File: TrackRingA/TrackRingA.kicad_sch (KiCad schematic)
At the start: 14 parts, among them J1 Conn_01x04, U1 TLV493D-A1B6, U2 LIS2DTW12

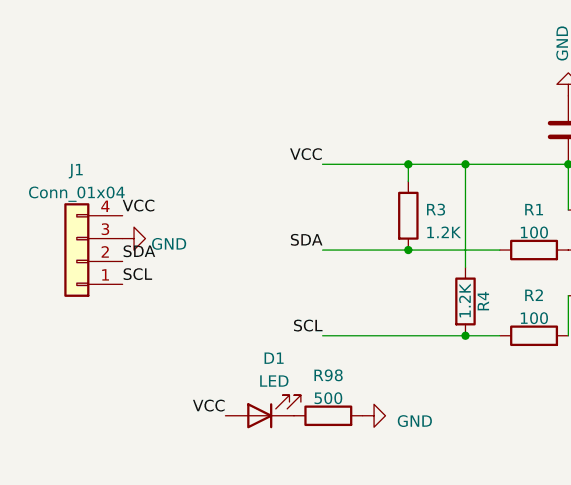
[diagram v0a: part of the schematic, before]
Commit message: Finished BusChain1.1 and added power daisy-chaining option
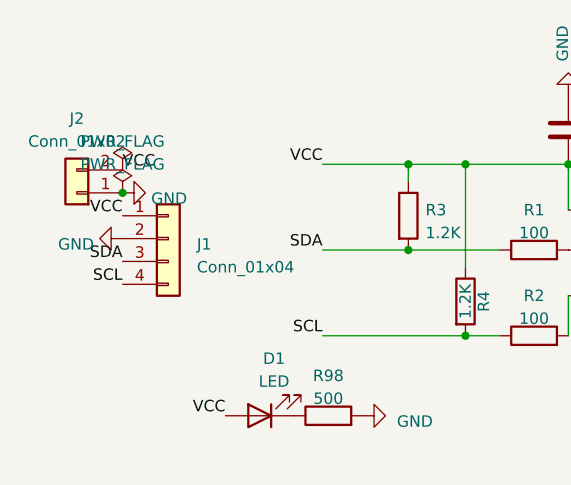
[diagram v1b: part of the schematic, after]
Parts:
- added J2: Conn_01x02, Connector_PinHeader_2.54mm:PinHeader_1x02_P2.54mm_Vertical, symbol Connector_Generic:Conn_01x02
- J1: footprint Connector_PinSocket_2.54mm:PinSocket_1x04_P2.54mm_Horizontal -> Connector_PinHeader_2.54mm:PinHeader_1x04_P2.54mm_Vertical
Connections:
- net GND: now also J1.2 (Pin_2), J2.1 (Pin_1); no longer J1.3 (Pin_3)
- net SCL: now also J1.4 (Pin_4); no longer J1.1 (Pin_1)
- net SDA: now also J1.3 (Pin_3); no longer J1.2 (Pin_2)
- net VCC: now also J1.1 (Pin_1), J2.2 (Pin_2); no longer J1.4 (Pin_4)
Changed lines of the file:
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@@
   (junction (at 92.075 91.44) (diameter 0) (color 0 0 0 0)
   )
+  (junction (at 27.305 31.115) (diameter 0) (color 0 0 0 0)
+  )
   (junction (at 76.2 66.04) (diameter 0) (color 0 0 0 0)
   )
@@
     (effects (font (size 1.27 1.27)) (justify right bottom))
   )
-  (label "SCL" (at 27.305 41.275 0) (fields_autoplaced)
+  (label "SCL" (at 27.305 41.275 180) (fields_autoplaced)
+    (effects (font (size 1.27 1.27)) (justify right bottom))
+  )
+  (label "VCC" (at 38.735 55.88 180) (fields_autoplaced)
+    (effects (font (size 1.27 1.27)) (justify right bottom))
+  )
+  (label "SCL" (at 49.53 46.99 180) (fields_autoplaced)
+    (effects (font (size 1.27 1.27)) (justify right bottom))
+  )
+  (label "SDA" (at 27.305 38.735 180) (fields_autoplaced)
+    (effects (font (size 1.27 1.27)) (justify right bottom))
+  )
+  (label "VCC" (at 88.9 66.04 180) (fields_autoplaced)
+    (effects (font (size 1.27 1.27)) (justify right bottom))
+  )
+  (label "VCC" (at 27.305 28.575 0) (fields_autoplaced)
     (effects (font (size 1.27 1.27)) (justify left bottom))
   )
-  (label "VCC" (at 38.735 55.88 180) (fields_autoplaced)
-    (effects (font (size 1.27 1.27)) (justify right bottom))
-  )
-  (label "SCL" (at 49.53 46.99 180) (fields_autoplaced)
-    (effects (font (size 1.27 1.27)) (justify right bottom))
-  )
-  (label "SDA" (at 27.305 38.735 0) (fields_autoplaced)
-    (effects (font (size 1.27 1.27)) (justify left bottom))
-  )
-  (label "VCC" (at 88.9 66.04 180) (fields_autoplaced)
-    (effects (font (size 1.27 1.27)) (justify right bottom))
-  )
-  (label "VCC" (at 27.305 33.655 0) (fields_autoplaced)
-    (effects (font (size 1.27 1.27)) (justify left bottom))
+  (label "VCC" (at 27.305 33.655 180) (fields_autoplaced)
+    (effects (font (size 1.27 1.27)) (justify right bottom))
+  )
+  (symbol (lib_id "Connector_Generic:Conn_01x04") (at 32.385 36.195 0) (unit 1)
+    (in_bom yes) (on_board yes) (dnp no) (fields_autoplaced)
+    (property "Reference" "J1" (at 35.56 36.83 0)
+      (effects (font (size 1.27 1.27)) (justify left))
+    )
+    (property "Value" "Conn_01x04" (at 35.56 39.37 0)
+      (effects (font (size 1.27 1.27)) (justify left))
+    )
+    (property "Footprint" "Connector_PinHeader_2.54mm:PinHeader_1x04_P2.54mm_Vertical" (at 32.385 36.195 0)
+      (effects (font (size 1.27 1.27)) hide)
+    )
+    (property "Datasheet" "~" (at 32.385 36.195 0)
+      (effects (font (size 1.27 1.27)) hide)
+    )
+    (pin "1")
+    (pin "2")
+    (pin "3")
+    (pin "4")
+    (instances
+      (project "TrackRingA"
+        (path "/1a22a45d-0453-4b94-9e49-dc92af99da64"
+          (reference "J1") (unit 1)
+        )
+      )
+    )
   )
   (symbol (lib_id "Device:R") (at 72.39 76.2 90) (unit 1)
@@
         (path "/1a22a45d-0453-4b94-9e49-dc92af99da64"
           (reference "R7") (unit 1)
+        )
+      )
+    )
+  )
+  (symbol (lib_id "power:GND") (at 27.305 31.115 90) (unit 1)
+    (in_bom yes) (on_board yes) (dnp no) (fields_autoplaced)
+    (property "Reference" "#PWR07" (at 33.655 31.115 0)
+      (effects (font (size 1.27 1.27)) hide)
+    )
+    (property "Value" "GND" (at 30.48 31.75 90)
+      (effects (font (size 1.27 1.27)) (justify right))
+    )
+    (property "Footprint" "" (at 27.305 31.115 0)
+      (effects (font (size 1.27 1.27)) hide)
+    )
+    (property "Datasheet" "" (at 27.305 31.115 0)
+      (effects (font (size 1.27 1.27)) hide)
+    )
+    (pin "1")
+    (instances
+      (project "TrackRingA"
+        (path "/1a22a45d-0453-4b94-9e49-dc92af99da64"
+          (reference "#PWR07") (unit 1)
         )
       )
@@
     )
   )
+  (symbol (lib_id "power:PWR_FLAG") (at 27.305 28.575 0) (unit 1)
+    (in_bom yes) (on_board yes) (dnp no) (fields_autoplaced)
+    (property "Reference" "#FLG01" (at 27.305 26.67 0)
+      (effects (font (size 1.27 1.27)) hide)
+    )
+    (property "Value" "PWR_FLAG" (at 27.305 25.4 0)
+      (effects (font (size 1.27 1.27)))
+    )
+    (property "Footprint" "" (at 27.305 28.575 0)
+      (effects (font (size 1.27 1.27)) hide)
+    )
+    (property "Datasheet" "~" (at 27.305 28.575 0)
+      (effects (font (size 1.27 1.27)) hide)
+    )
+    (pin "1")
+    (instances
+      (project "TrackRingA"
+        (path "/1a22a45d-0453-4b94-9e49-dc92af99da64"
+          (reference "#FLG01") (unit 1)
+        )
+      )
+    )
+  )
   (symbol (lib_id "Device:R") (at 50.165 55.88 90) (unit 1)
     (in_bom yes) (on_board yes) (dnp no) (fields_autoplaced)
@@
         (path "/1a22a45d-0453-4b94-9e49-dc92af99da64"
           (reference "#PWR01") (unit 1)
+        )
+      )
+    )
+  )
+  (symbol (lib_id "power:PWR_FLAG") (at 27.305 31.115 0) (unit 1)
+    (in_bom yes) (on_board yes) (dnp no) (fields_autoplaced)
+    (property "Reference" "#FLG02" (at 27.305 29.21 0)
+      (effects (font (size 1.27 1.27)) hide)
+    )
+    (property "Value" "PWR_FLAG" (at 27.305 27.94 0)
+      (effects (font (size 1.27 1.27)))
+    )
+    (property "Footprint" "" (at 27.305 31.115 0)
+      (effects (font (size 1.27 1.27)) hide)
+    )
+    (property "Datasheet" "~" (at 27.305 31.115 0)
+      (effects (font (size 1.27 1.27)) hide)
+    )
+    (pin "1")
+    (instances
+      (project "TrackRingA"
+        (path "/1a22a45d-0453-4b94-9e49-dc92af99da64"
+          (reference "#FLG02") (unit 1)
+        )
+      )
+    )
+  )
+  (symbol (lib_id "Connector_Generic:Conn_01x02") (at 22.225 31.115 180) (unit 1)
+    (in_bom yes) (on_board yes) (dnp no) (fields_autoplaced)
+    (property "Reference" "J2" (at 22.225 22.86 0)
+      (effects (font (size 1.27 1.27)))
+    )
+    (property "Value" "Conn_01x02" (at 22.225 25.4 0)
+      (effects (font (size 1.27 1.27)))
+    )
+    (property "Footprint" "Connector_PinHeader_2.54mm:PinHeader_1x02_P2.54mm_Vertical" (at 22.225 31.115 0)
+      (effects (font (size 1.27 1.27)) hide)
+    )
+    (property "Datasheet" "~" (at 22.225 31.115 0)
+      (effects (font (size 1.27 1.27)) hide)
+    )
+    (pin "1")
+    (pin "2")
+    (instances
+      (project "TrackRingA"
+        (path "/1a22a45d-0453-4b94-9e49-dc92af99da64"
+          (reference "J2") (unit 1)
         )
       )
@@
     )
   )
-  (symbol (lib_id "Connector_Generic:Conn_01x04") (at 22.225 38.735 180) (unit 1)
-    (in_bom yes) (on_board yes) (dnp no) (fields_autoplaced)
-    (property "Reference" "J1" (at 22.225 28.575 0)
-      (effects (font (size 1.27 1.27)))
-    )
-    (property "Value" "Conn_01x04" (at 22.225 31.115 0)
-      (effects (font (size 1.27 1.27)))
-    )
-    (property "Footprint" "Connector_PinSocket_2.54mm:PinSocket_1x04_P2.54mm_Horizontal" (at 22.225 38.735 0)
-      (effects (font (size 1.27 1.27)) hide)
-    )
-    (property "Datasheet" "~" (at 22.225 38.735 0)
-      (effects (font (size 1.27 1.27)) hide)
-    )
-    (pin "1")
-    (pin "2")
-    (pin "3")
-    (pin "4")
-    (instances
-      (project "TrackRingA"
-        (path "/1a22a45d-0453-4b94-9e49-dc92af99da64"
-          (reference "J1") (unit 1)
-        )
-      )
-    )
-  )
   (symbol (lib_id "Device:LED") (at 42.545 55.88 180) (unit 1)
     (in_bom yes) (on_board yes) (dnp no) (fields_autoplaced)
@@
     )
   )
-  (symbol (lib_id "power:GND") (at 27.305 36.195 90) (unit 1)
-    (in_bom yes) (on_board yes) (dnp no) (fields_autoplaced)
-    (property "Reference" "#PWR02" (at 33.655 36.195 0)
-      (effects (font (size 1.27 1.27)) hide)
-    )
-    (property "Value" "GND" (at 30.48 36.83 90)
+  (symbol (lib_id "power:GND") (at 27.305 36.195 270) (unit 1)
+    (in_bom yes) (on_board yes) (dnp no) (fields_autoplaced)
+    (property "Reference" "#PWR02" (at 20.955 36.195 0)
+      (effects (font (size 1.27 1.27)) hide)
+    )
+    (property "Value" "GND" (at 24.13 36.83 90)
       (effects (font (size 1.27 1.27)) (justify right))
     )
